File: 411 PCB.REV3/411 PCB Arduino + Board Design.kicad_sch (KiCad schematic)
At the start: 30 parts, among them J1 ICSP CONN, J2 Conn_01x06_MountingPin, J4 Conn_01x04, Q1 Q_NMOS_GDS, SW1 SW_SPST, SW3 SW_MEC_5E, U1 ATmega328P-P, Y1 8 MHz

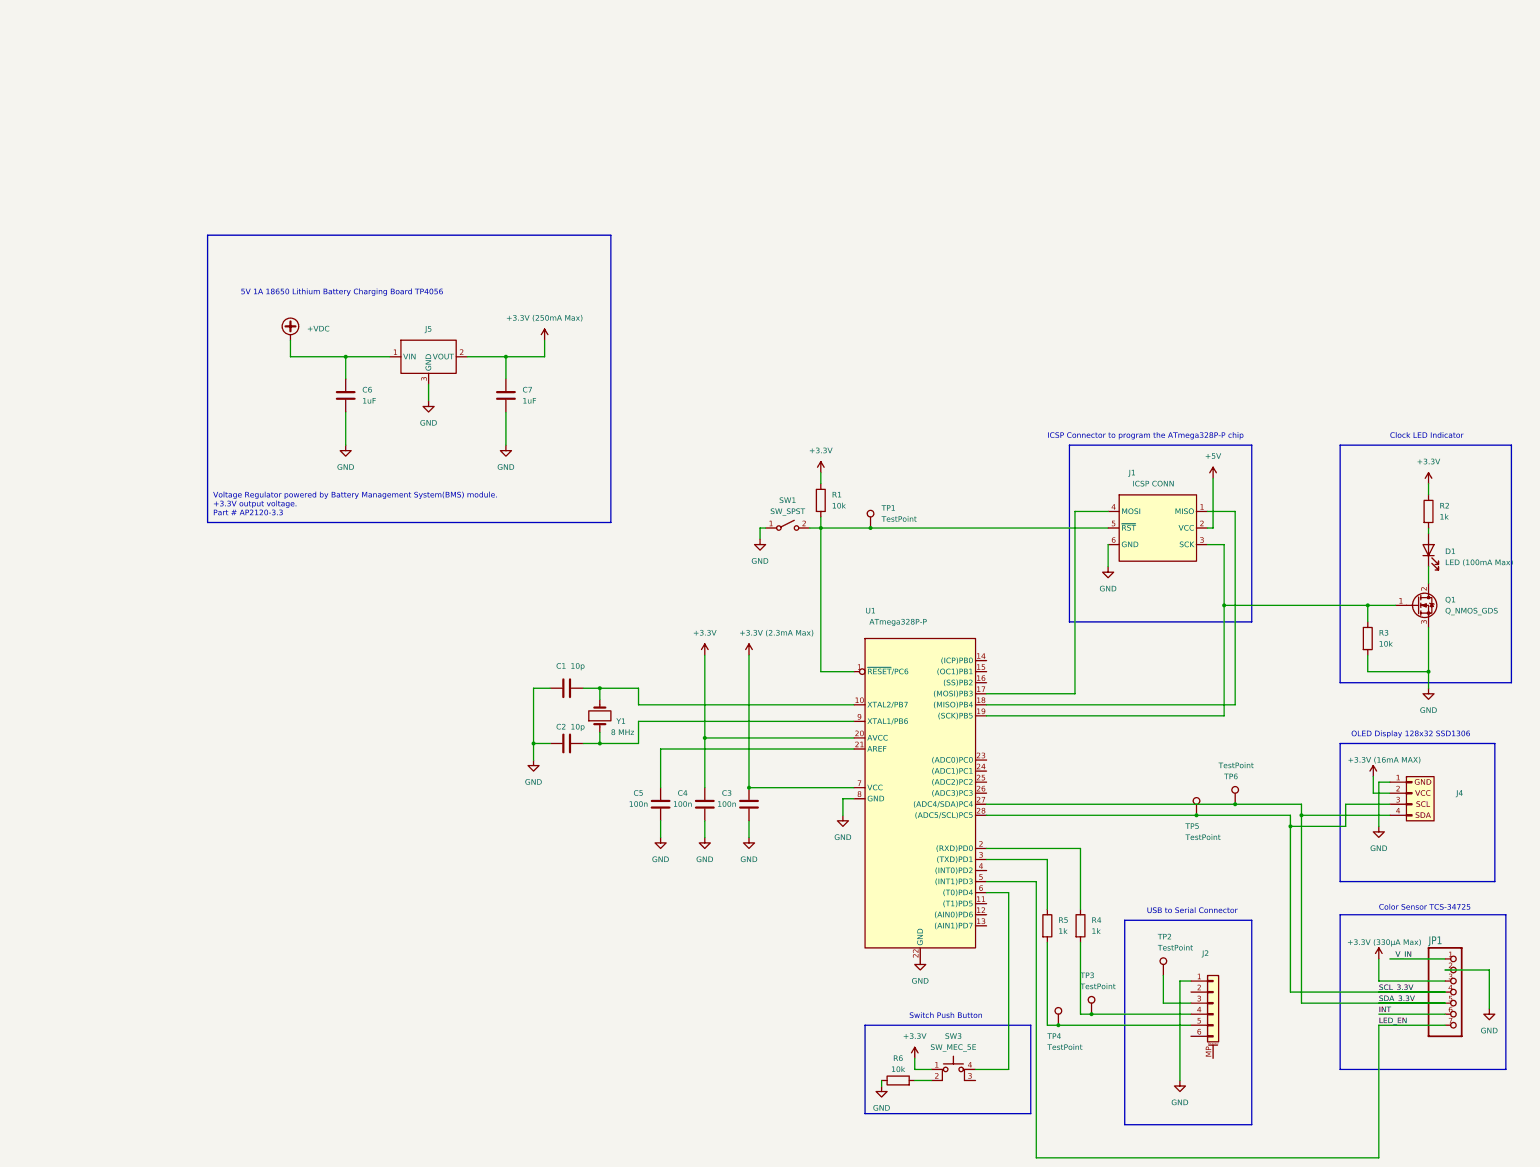
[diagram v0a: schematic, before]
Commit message: New Schematic for Rev 3 and updated BOM
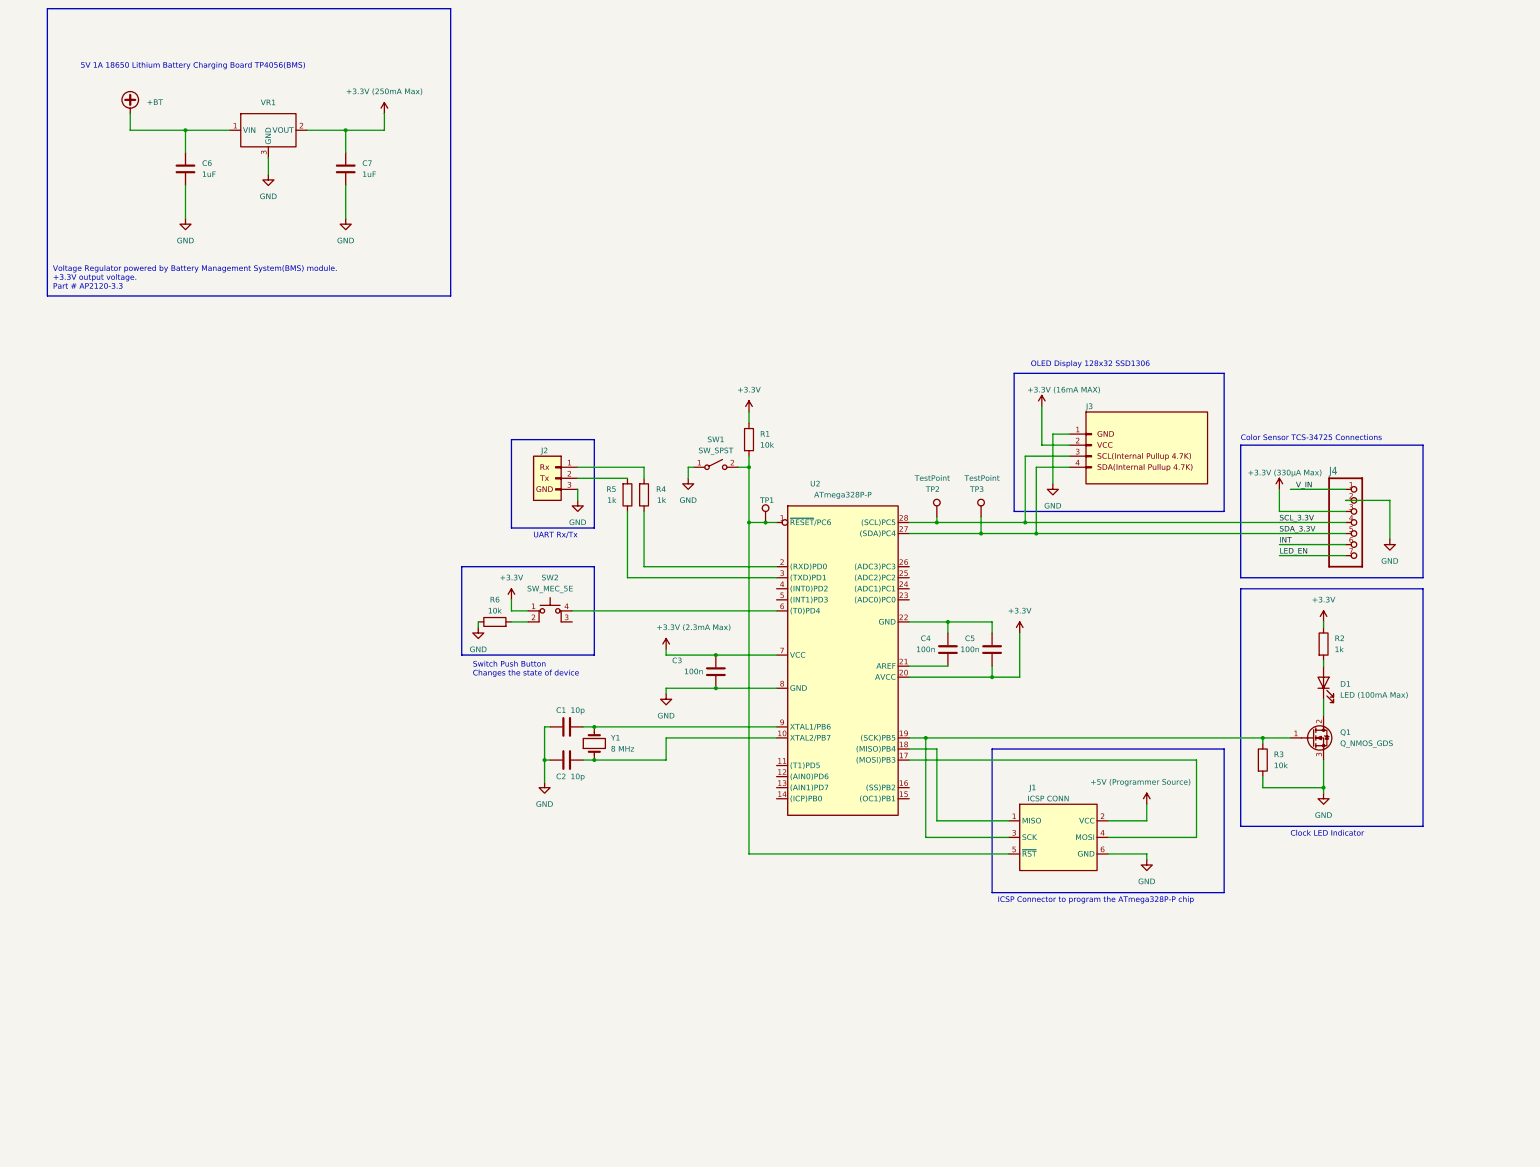
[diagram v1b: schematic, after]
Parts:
- removed J2: Conn_01x06_MountingPin, Connector_PinHeader_2.00mm:PinHeader_1x06_P2.00mm_Vertical, symbol Connector_Generic_MountingPin:Conn_01x06_MountingPin
- removed J4: Conn_01x04, Connector_PinHeader_1.00mm:PinHeader_1x04_P1.00mm_Vertical, symbol Connector_Generic:Conn_01x04
- removed JP1: HEADER-1X770MIL, Connector_PinHeader_1.27mm:PinHeader_1x07_P1.27mm_Vertical, symbol Adafruit TCS34725-eagle-import:HEADER-1X770MIL
- removed SW3: SW_MEC_5E, Button_Switch_THT:SW_PUSH_6mm, symbol Switch:SW_MEC_5E
- removed TP4, TP5, TP6: TestPoint, Connector_PinHeader_1.00mm:PinHeader_1x01_P1.00mm_Vertical, symbol Connector:TestPoint
- removed U1: ATmega328P-P, Package_DIP:DIP-28_W7.62mm, symbol MCU_Microchip_ATmega:ATmega328P-P
- added J2: ~, symbol Connector_Generic:Conn_01x03
- added J3: Conn_01x04, Connector_PinHeader_1.00mm:PinHeader_1x04_P1.00mm_Vertical, symbol Connector_Generic:Conn_01x04
- added J4: HEADER-1X770MIL, Connector_PinHeader_1.27mm:PinHeader_1x07_P1.27mm_Vertical, symbol Adafruit TCS34725-eagle-import:HEADER-1X770MIL
- added SW2: SW_MEC_5E, Button_Switch_THT:SW_PUSH_6mm, symbol Switch:SW_MEC_5E
- added U2: ATmega328P-P, Package_DIP:DIP-28_W7.62mm, symbol MCU_Microchip_ATmega:ATmega328P-P
- renumbered J5 to VR1
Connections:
- net +3.3V: now also C5.1, J3.2 (Pin_2), J4.3, SW2.1, U2.20 (AVCC), U2.7 (VCC); no longer C4.2
- net GND: now also J2.3 (Pin_3), J3.1 (Pin_1), J4.2, U2.8 (GND); no longer C4.1, C5.1
- net INT: now also J4.6
- net LED_EN: now also J4.7
- net SCL_3.3V: now also TP2.1, J3.3 (Pin_3), J4.4, U2.28 ((SCL)PC5)
- net SDA_3.3V: now also TP3.1, J3.4 (Pin_4), J4.5, U2.27 ((SDA)PC4)
- net V_IN: now also J4.1
- net at R6.2: now also SW2.2
- net at R5.1: now also U2.3 ((TXD)PD1)
- net at R5.2: now also J2.2 (Pin_2)
- net at C2.2, Y1.1: now also U2.10 (XTAL2/PB7)
- net at C1.2, Y1.2: now also U2.9 (XTAL1/PB6)
- net at R4.2: now also J2.1 (Pin_1); no longer TP3.1
- net at J1.1 (MISO): now also U2.18 ((MISO)PB4)
- net at J1.3 (SCK), Q1.1 (G), R3.1: now also U2.19 ((SCK)PB5)
- net at J1.4 (MOSI): now also U2.17 ((MOSI)PB3)
- net at J1.5 (~{RST}), R1.2, SW1.2 (B)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: now also U2.1 (~{RESET}/PC6)
- net at R4.1: now also U2.2 ((RXD)PD0)
- net at C5.2: now also C4.2, U2.22 (GND)
- new net: SW2.4 (A), U2.6 ((T0)PD4)
- new net: C4.1, U2.21 (AREF)
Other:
- note added: "5V 1A 18650 Lithium Battery Charging Board TP4056(BMS)"
- note added: "Color Sensor TCS-34725 Connections"
- note added: "Switch Push Button Changes the state of device"
- note added: "UART Rx/Tx"
- note removed: "5V 1A 18650 Lithium Battery Charging Board TP4056"
- note removed: "Color Sensor TCS-34725"
- note removed: "Switch Push Button"
- note removed: "USB to Serial Connector"
- moved on the sheet: C6, C7, VR1

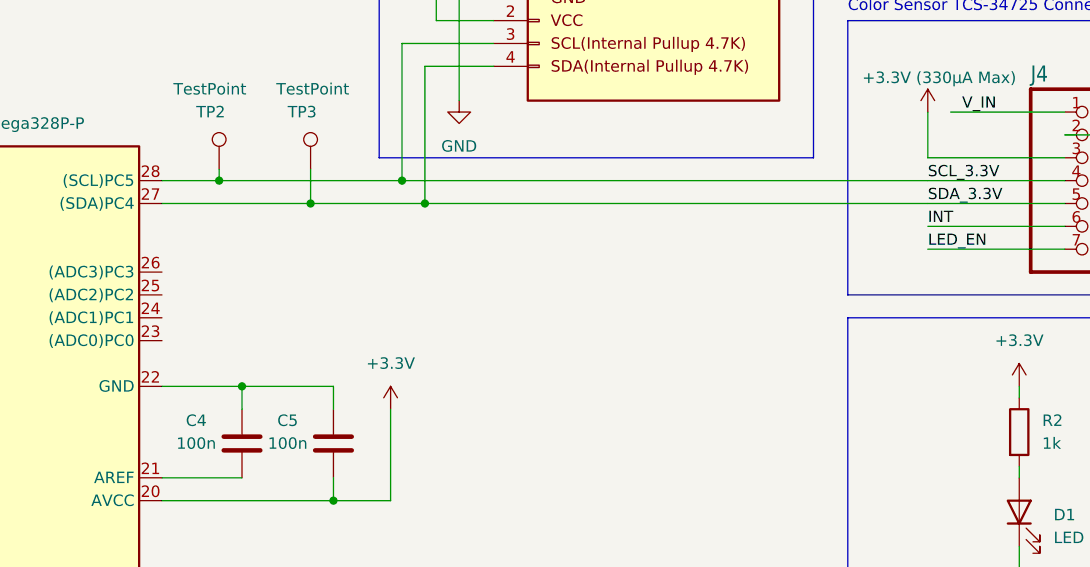
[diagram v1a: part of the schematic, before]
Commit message: added LED connection for RGB Sensor
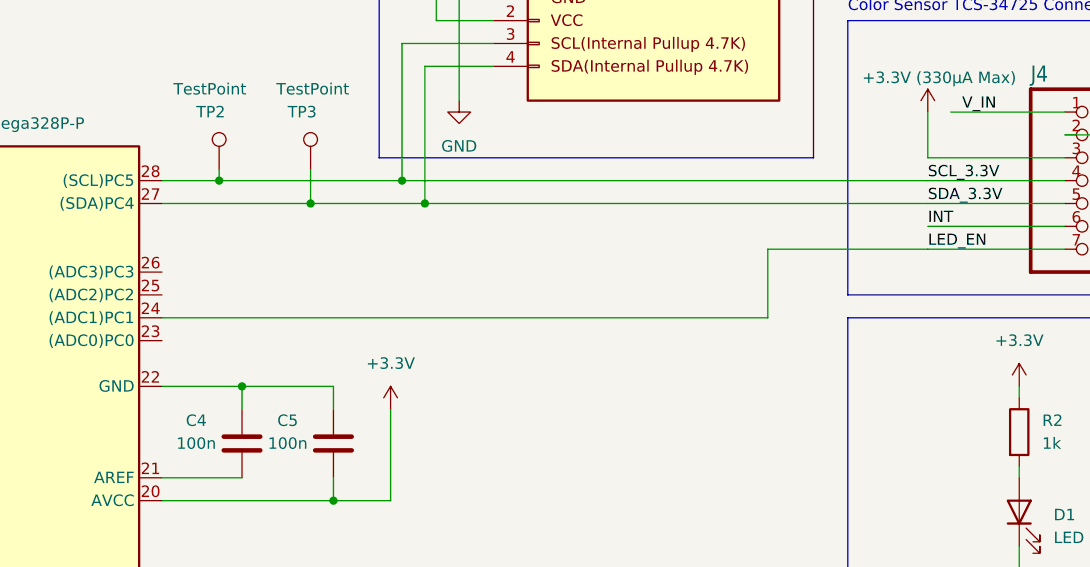
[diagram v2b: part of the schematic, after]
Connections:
- net LED_EN: now also U2.24 ((ADC1)PC1)
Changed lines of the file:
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@@
+    (stroke (width 0) (type default))
+  )
+  (wire (pts (xy 298.45 204.47) (xy 365.76 204.47))
     (stroke (width 0) (type default))
   )
@@
     (stroke (width 0) (type default))
   )
+  (wire (pts (xy 365.76 196.85) (xy 383.54 196.85))
+    (stroke (width 0) (type default))
+  )
   (wire (pts (xy 261.62 189.23) (xy 261.62 265.43))
     (stroke (width 0) (type default))
@@
     (stroke (width 0) (type default))
   )
+  (wire (pts (xy 365.76 204.47) (xy 365.76 196.85))
+    (stroke (width 0) (type default))
+  )
